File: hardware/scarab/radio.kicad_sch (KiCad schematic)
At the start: 22 parts, among them U1 A7105, Y1 16mhz Seiko Epson Q24FA20H005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

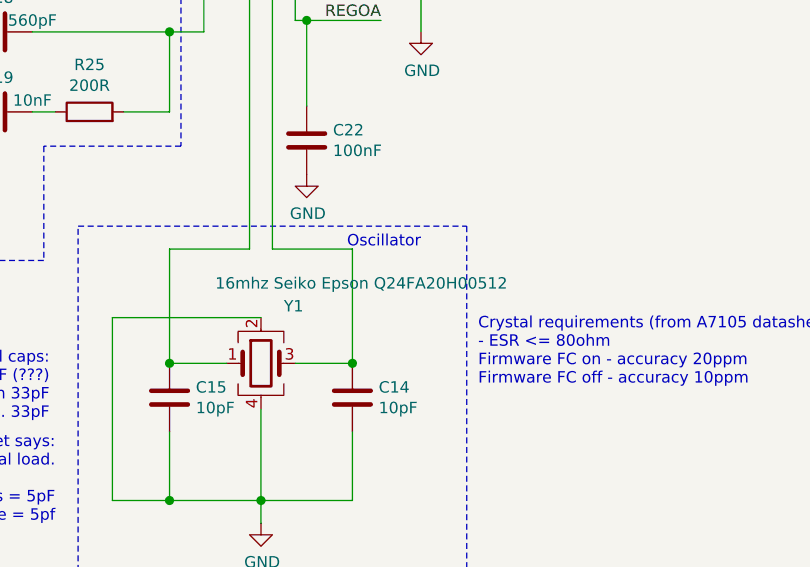
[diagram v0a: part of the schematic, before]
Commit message: Silkscreen art; fix crystal part number
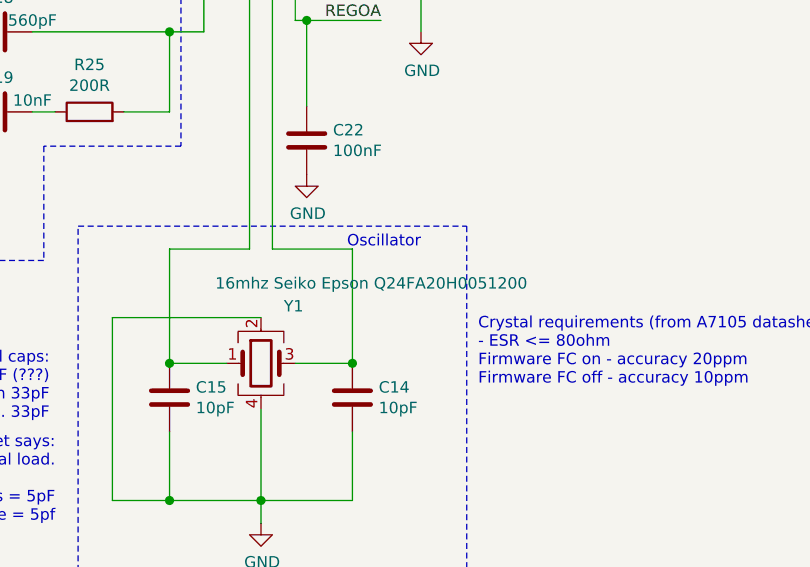
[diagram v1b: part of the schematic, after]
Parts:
- Y1: value 16mhz Seiko Epson Q24FA20H00512 -> 16mhz Seiko Epson Q24FA20H0051200; MPN Q24FA20H00512 -> Q24FA20H0051200
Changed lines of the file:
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@@
       (effects (font (size 1.27 1.27)) (justify left))
     )
-    (property "Value" "16mhz Seiko Epson Q24FA20H00512" (at 213.36 128.27 0)
+    (property "Value" "16mhz Seiko Epson Q24FA20H0051200" (at 213.36 128.27 0)
       (effects (font (size 1.27 1.27)) (justify left))
     )
@@
       (effects (font (size 1.27 1.27)) hide)
     )
-    (property "MPN" "Q24FA20H00512" (at 218.44 137.16 0)
+    (property "MPN" "Q24FA20H0051200" (at 218.44 137.16 0)
       (effects (font (size 1.27 1.27)) hide)
     )
